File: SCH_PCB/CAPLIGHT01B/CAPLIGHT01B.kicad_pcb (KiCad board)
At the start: 2 copper layers, 33 x 20.3 mm, 14 parts, among them J1 JUMP_3X2, P1 USB_OTG, U1 LTC3625

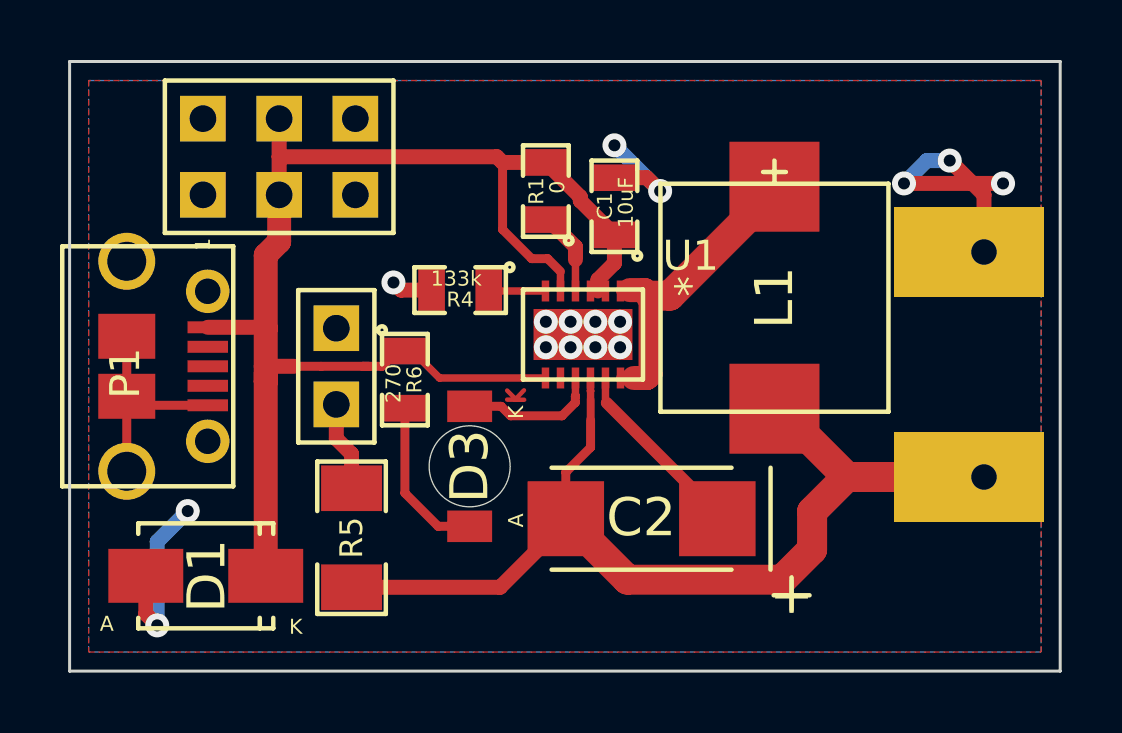
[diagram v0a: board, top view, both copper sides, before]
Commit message: Improved PCB layout for easier manufacturing.
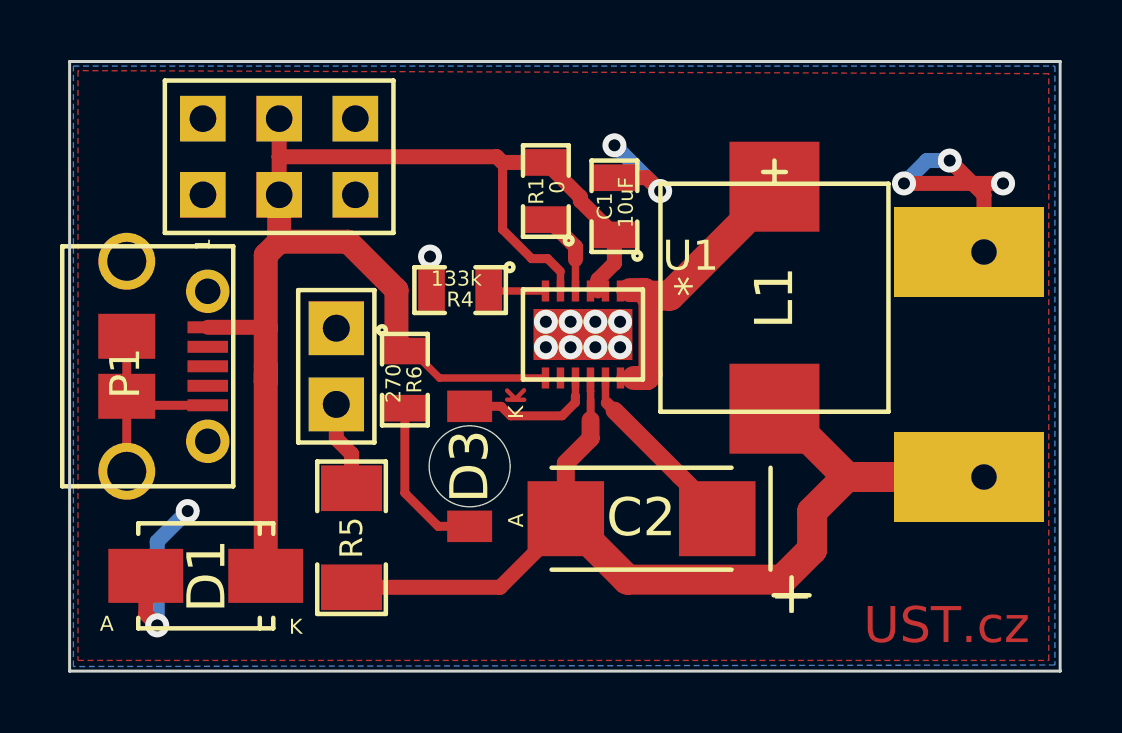
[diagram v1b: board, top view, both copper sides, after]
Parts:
- added G***: LOGO, graphics:UST_logo, B.Cu at (158.4, 113.8)
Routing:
- net /VIN: track 49.3 -> 50.0 mm
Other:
- board text added: "CAPLIGHT01B"
- board text removed: "CAPLIGHT01A"

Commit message: Opravy výrobní data
Generována nová data. Zvětšen otvor pro C 50F.
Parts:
- C3: footprint Mlab_C:C_Radial_D18_L25_P7.5 -> Mlab_C:C_Radial_D18_L25_P7.5_BAT
- moved C3 0.25 mm to (168.0, 121.8)
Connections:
- P1 pad 2: Net-(P1-Pad2) -> (no net)
- P1 pad 3: Net-(P1-Pad3) -> (no net)
- P1 pad 4: Net-(P1-Pad4) -> (no net)
- U1 pad 8: Net-(U1-Pad8) -> (no net)
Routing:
- net Net-(C2-Pad2): track 40.6 -> 44.9 mm
- net (no net): track 13.1 -> 9.53 mm
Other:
- rule pad_to_mask_clearance: 0 -> 0.2
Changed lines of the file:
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@@
-(kicad_pcb (version 20160815) (host pcbnew 4.1.0-alpha+201608181240+7066~46~ubuntu16.04.1-product)
+(kicad_pcb (version 20160815) (host pcbnew "(2016-09-17 revision 679eef1)-makepkg")
   (general
     (links 45)
     (no_connects 0)
-    (area 131.754999 102.075 182.244001 130.52232)
+    (area 137.744999 107.899999 170.865001 128.320001)
     (thickness 1.6)
     (drawings 20)
-    (tracks 139)
+    (tracks 140)
     (zones 0)
     (modules 15)
-    (nets 15)
+    (nets 11)
   )
   (page A4)
@@
   )
   (setup
-    (last_trace_width 0.5)
+    (last_trace_width 1)
     (user_trace_width 0.25)
     (user_trace_width 0.3)
@@
     (pad_size 3 5)
     (pad_drill 0.85)
-    (pad_to_mask_clearance 0)
+    (pad_to_mask_clearance 0.2)
+    (solder_mask_min_width 0.2)
     (aux_axis_origin 137.795 128.27)
-    (visible_elements FFFFFF7F)
+    (visible_elements 7FFFFFFF)
     (pcbplotparams
       (layerselection 0x010d0_ffffffff)
@@
   (net 9 "Net-(D3-Pad2)")
   (net 10 /PG)
-  (net 11 "Net-(P1-Pad3)")
-  (net 12 "Net-(P1-Pad2)")
-  (net 13 "Net-(P1-Pad4)")
-  (net 14 "Net-(U1-Pad8)")
   (net_class Default "This is the default net class."
     (clearance 0.2)
@@
     (add_net "Net-(D2-Pad2)")
     (add_net "Net-(D3-Pad2)")
-    (add_net "Net-(P1-Pad2)")
-    (add_net "Net-(P1-Pad3)")
-    (add_net "Net-(P1-Pad4)")
     (add_net "Net-(R1-Pad1)")
     (add_net "Net-(R4-Pad1)")
-    (add_net "Net-(U1-Pad8)")
   )
   (net_class thick ""
@@
     (add_net "Net-(L1-Pad1)")
   )
+  (module Mlab_C:C_Radial_D18_L25_P7.5_BAT (layer B.Cu)
+    (at 168.021 121.793 90)
+    (descr "Radial Electrolytic Capacitor Diameter 16mm x Length 25mm, Pitch 7.5mm")
+    (tags "Electrolytic Capacitor")
+    (fp_text reference C3 (at 4.071 -0.254 90) (layer B.SilkS)
+      (effects (font (size 1 1) (thickness 0.15)) (justify mirror))
+    )
+    (fp_text value 50F (at 3.75 -9.3 90) (layer B.Fab) hide
+      (effects (font (size 1 1) (thickness 0.15)) (justify mirror))
+    )
+    (fp_text user + (at -0.0381 -2.54 90) (layer B.SilkS)
+      (effects (font (size 1.5 1.5) (thickness 0.15)) (justify mirror))
+    )
+    (fp_circle (center 7.5 0) (end 7.5 1) (layer B.SilkS) (width 0.15))
+    (fp_circle (center 3.75 0) (end 3.75 -9) (layer B.CrtYd) (width 0.05))
+    (pad 1 thru_hole rect (at 0 0 90) (size 3 5) (drill 0.95 (offset 0 -0.5)) (layers *.Cu *.Mask B.SilkS)
+      (net 5 "Net-(C2-Pad2)"))
+    (pad 2 thru_hole rect (at 7.5 0 90) (size 3 5) (drill 0.95 (offset 0 -0.5)) (layers *.Cu *.Mask B.SilkS)
+      (net 2 GND))
+    (model Capacitors_ThroughHole.3dshapes/C_Radial_D16_L25_P7.5.wrl
+      (at (xyz 0.147638 0 0))
+      (scale (xyz 1 1 1))
+      (rotate (xyz 0 0 90))
+    )
+  )
   (module Mlab_Pin_Headers:Straight_1x02 (layer F.Cu)
     (at 146.685 118.11)
@@
     (model Pin_Headers/Pin_Header_Straight_1x02.wrl
       (at (xyz 0 0 0))
-      (scale (xyz 1 1 1))
-      (rotate (xyz 0 0 90))
-    )
-  )
-  (module Mlab_C:C_Radial_D18_L25_P7.5 (layer B.Cu)
-    (at 168.275 121.8 90)
-    (descr "Radial Electrolytic Capacitor Diameter 16mm x Length 25mm, Pitch 7.5mm")
-    (tags "Electrolytic Capacitor")
-    (fp_text reference C3 (at 4.071 -0.254 90) (layer B.SilkS)
-      (effects (font (size 1 1) (thickness 0.15)) (justify mirror))
-    )
-    (fp_text value 50F (at 3.75 -9.3 90) (layer B.Fab) hide
-      (effects (font (size 1 1) (thickness 0.15)) (justify mirror))
-    )
-    (fp_text user + (at -0.0381 -2.54 90) (layer B.SilkS)
-      (effects (font (size 1.5 1.5) (thickness 0.15)) (justify mirror))
-    )
-    (fp_circle (center 7.5 0) (end 7.5 1) (layer B.SilkS) (width 0.15))
-    (fp_circle (center 3.75 0) (end 3.75 -9) (layer B.CrtYd) (width 0.05))
-    (pad 1 thru_hole rect (at 0 0 90) (size 3 5) (drill 0.85 (offset 0 -0.5)) (layers *.Cu *.Mask B.SilkS)
-      (net 5 "Net-(C2-Pad2)"))
-    (pad 2 thru_hole rect (at 7.5 0 90) (size 3 5) (drill 0.85 (offset 0 -0.5)) (layers *.Cu *.Mask B.SilkS)
-      (net 2 GND))
-    (model Capacitors_ThroughHole.3dshapes/C_Radial_D16_L25_P7.5.wrl
-      (at (xyz 0.147638 0 0))
       (scale (xyz 1 1 1))
       (rotate (xyz 0 0 90))
@@
     (pad 7 smd rect (at 1.45 1.25 270) (size 0.7 0.25) (layers F.Cu F.Paste F.Mask)
       (net 1 /VIN))
-    (pad 8 smd rect (at 1.45 0.75 270) (size 0.7 0.25) (layers F.Cu F.Paste F.Mask)
-      (net 14 "Net-(U1-Pad8)"))
+    (pad 8 smd rect (at 1.45 0.75 270) (size 0.7 0.25) (layers F.Cu F.Paste F.Mask))
     (pad 9 smd rect (at 1.45 0.25 270) (size 0.7 0.25) (layers F.Cu F.Paste F.Mask)
       (net 10 /PG))
@@
     (pad 5 thru_hole circle (at 2.5 -2.7 270) (size 1.45 1.45) (drill 0.85) (layers *.Cu *.Mask)
       (net 2 GND))
-    (pad 3 smd trapezoid (at 0 -2.7 270) (size 0.4 1.35) (layers F.Cu F.Mask)
-      (net 11 "Net-(P1-Pad3)"))
-    (pad 2 smd trapezoid (at -0.65 -2.7 270) (size 0.4 1.35) (layers F.Cu F.Mask)
-      (net 12 "Net-(P1-Pad2)"))
+    (pad 3 smd trapezoid (at 0 -2.7 270) (size 0.4 1.35) (layers F.Cu F.Mask))
+    (pad 2 smd trapezoid (at -0.65 -2.7 270) (size 0.4 1.35) (layers F.Cu F.Mask))
     (pad 1 smd trapezoid (at -1.3 -2.7 270) (size 0.4 1.35) (layers F.Cu F.Mask)
       (net 1 /VIN))
-    (pad 4 smd trapezoid (at 0.65 -2.7 270) (size 0.4 1.35) (layers F.Cu F.Mask)
-      (net 13 "Net-(P1-Pad4)"))
+    (pad 4 smd trapezoid (at 0.65 -2.7 270) (size 0.4 1.35) (layers F.Cu F.Mask))
     (pad 5 smd trapezoid (at 1.3 -2.7 270) (size 0.4 1.35) (layers F.Cu F.Mask)
       (net 2 GND))
@@
   (gr_line (start 137.795 128.27) (end 170.815 128.27) (angle 90) (layer Edge.Cuts) (width 0.1))
   (segment (start 176.53 130.175) (end 176.53 120.65) (width 0.25) (layer Dwgs.User) (net 0))
-  (segment (start 132.08 113.03) (end 134.62 110.49) (width 0.25) (layer Dwgs.User) (net 0))
   (segment (start 144.78 113.957) (end 147.0786 113.957) (width 0.8) (layer F.Cu) (net 1))
   (segment (start 148.6916 115.57) (end 148.6916 117.3226) (width 0.8) (layer F.Cu) (net 1))
@@
   (segment (start 154.1575 115.6) (end 154.1575 114.95) (width 0.25) (layer F.Cu) (net 1))
   (segment (start 154.1575 114.95) (end 153.728999 114.521499) (width 0.3) (layer F.Cu) (net 1))
-  (segment (start 149.8092 115.018085) (end 149.8092 114.4524) (width 0.5) (layer F.Cu) (net 2))
-  (segment (start 149.8092 115.5192) (end 149.8092 115.018085) (width 0.5) (layer F.Cu) (net 2))
-  (segment (start 149.86 115.57) (end 149.8092 115.5192) (width 0.5) (layer F.Cu) (net 2))
-  (via (at 149.8092 114.4524) (size 0.8) (drill 0.4) (layers F.Cu B.Cu) (net 2))
   (segment (start 165.608 112.014) (end 168.91 112.014) (width 0.5) (layer F.Cu) (net 2))
   (via (at 168.91 112.014) (size 0.8) (drill 0.4) (layers F.Cu B.Cu) (net 2))
@@
   (segment (start 168.275 112.395) (end 167.132 111.252) (width 0.5) (layer F.Cu) (net 2))
   (via (at 167.132 111.252) (size 0.8) (drill 0.4) (layers F.Cu B.Cu) (net 2))
+  (segment (start 149.8092 115.018085) (end 149.8092 114.4524) (width 0.5) (layer F.Cu) (net 2))
+  (segment (start 149.8092 115.5192) (end 149.8092 115.018085) (width 0.5) (layer F.Cu) (net 2))
+  (segment (start 149.86 115.57) (end 149.8092 115.5192) (width 0.5) (layer F.Cu) (net 2))
+  (via (at 149.8092 114.4524) (size 0.8) (drill 0.4) (layers F.Cu B.Cu) (net 2))
   (segment (start 140.716 126.746) (end 140.716 123.952) (width 0.5) (layer B.Cu) (net 2))
   (segment (start 140.716 123.952) (end 141.732 122.936) (width 0.5) (layer B.Cu) (net 2))
@@
   (segment (start 159.385 123.19) (end 159.385 123.063) (width 0.4) (layer F.Cu) (net 4))
   (segment (start 159.3596 123.19) (end 159.385 123.19) (width 0.3) (layer F.Cu) (net 4))
+  (segment (start 163.696 121.8) (end 168.014 121.8) (width 1) (layer F.Cu) (net 5))
+  (segment (start 168.014 121.8) (end 168.021 121.793) (width 1) (layer F.Cu) (net 5))
   (segment (start 154.33548 123.19) (end 154.33548 121.34032) (width 0.6) (layer F.Cu) (net 5))
   (segment (start 154.33548 121.34032) (end 155.16101 120.51479) (width 0.6) (layer F.Cu) (net 5))
